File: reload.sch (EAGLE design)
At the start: 19 parts, among them IC1 LP2950, IC2 LP2950Z, Q1 BTS117

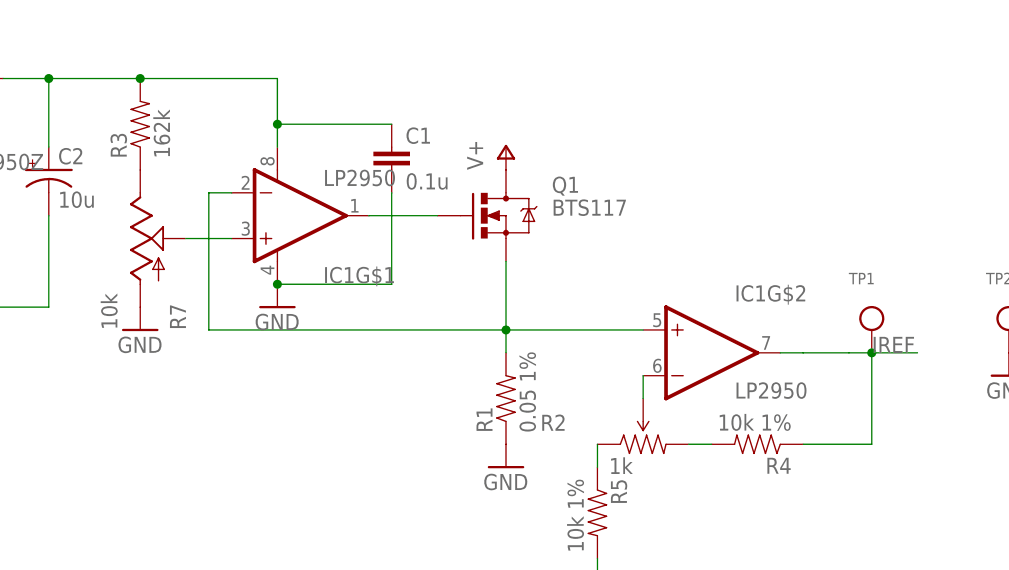
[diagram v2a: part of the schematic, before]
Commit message: Added a second BoM for 10A version.
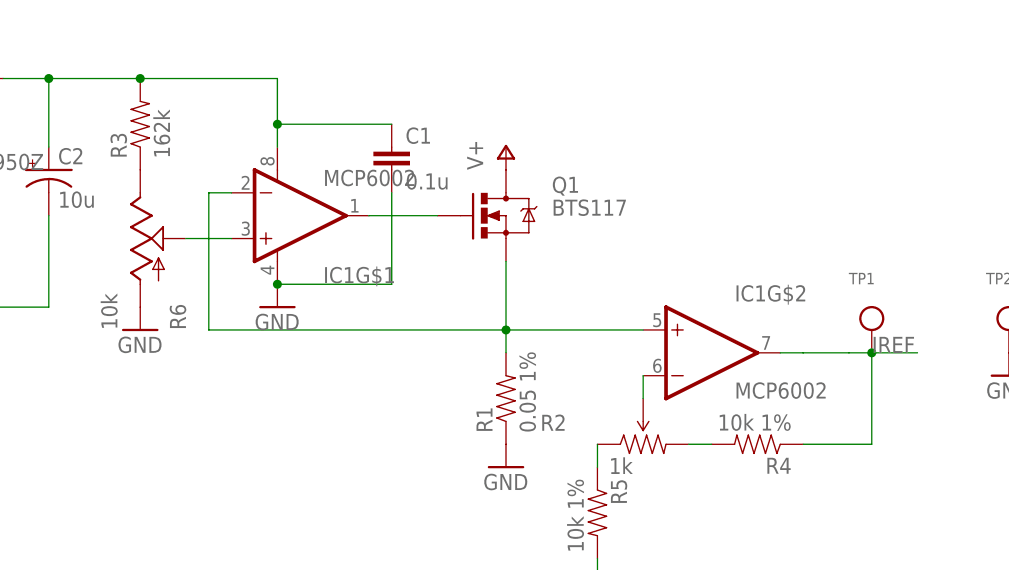
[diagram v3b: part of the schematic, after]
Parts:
- IC1: value LP2950 -> MCP6002
- renumbered R7 to R6
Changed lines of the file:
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@@
 </classes>
 <parts>
-<part name="IC1" library="SparkFun-AnalogIC" deviceset="LM358" device="" value="LP2950"/>
+<part name="IC1" library="SparkFun-AnalogIC" deviceset="LM358" device="" value="MCP6002"/>
 <part name="R1" library="SparkFun-Passives" deviceset="RESISTOR" device="PTH-1W" value="0.05 1%"/>
 <part name="Q1" library="SparkFun-DiscreteSemi" deviceset="MOSFET-NCHANNEL" device="PTH2" value="BTS117"/>
@@
 <part name="GND1" library="supply1" deviceset="GND" device=""/>
 <part name="GND2" library="supply1" deviceset="GND" device=""/>
-<part name="R7" library="SparkFun-Electromechanical" deviceset="POT" device="" value="10k"/>
+<part name="R6" library="SparkFun-Electromechanical" deviceset="POT" device="" value="10k"/>
 <part name="GND3" library="supply1" deviceset="GND" device=""/>
 <part name="R3" library="SparkFun-Passives" deviceset="RESISTOR" device="AXIAL-0.3" value="162k"/>
@@
 <instance part="GND1" gate="1" x="58.42" y="7.62"/>
 <instance part="GND2" gate="1" x="33.02" y="25.4"/>
-<instance part="R7" gate="G$1" x="17.78" y="33.02"/>
+<instance part="R6" gate="G$1" x="17.78" y="33.02"/>
 <instance part="GND3" gate="1" x="17.78" y="22.86"/>
 <instance part="R3" gate="G$1" x="17.78" y="45.72" rot="R90"/>
@@
 </segment>
 <segment>
-<pinref part="R7" gate="G$1" pin="A"/>
+<pinref part="R6" gate="G$1" pin="A"/>
 <pinref part="GND3" gate="1" pin="GND"/>
 </segment>
@@
 <net name="N$3" class="0">
 <segment>
-<pinref part="R7" gate="G$1" pin="E"/>
+<pinref part="R6" gate="G$1" pin="E"/>
 <pinref part="R3" gate="G$1" pin="1"/>
 </segment>
@@
 <net name="N$4" class="0">
 <segment>
-<pinref part="R7" gate="G$1" pin="S"/>
+<pinref part="R6" gate="G$1" pin="S"/>
 <pinref part="IC1" gate="G$1" pin="+IN"/>
 <wire x1="22.86" y1="33.02" x2="27.94" y2="33.02" width="0.1524" layer="91"/>

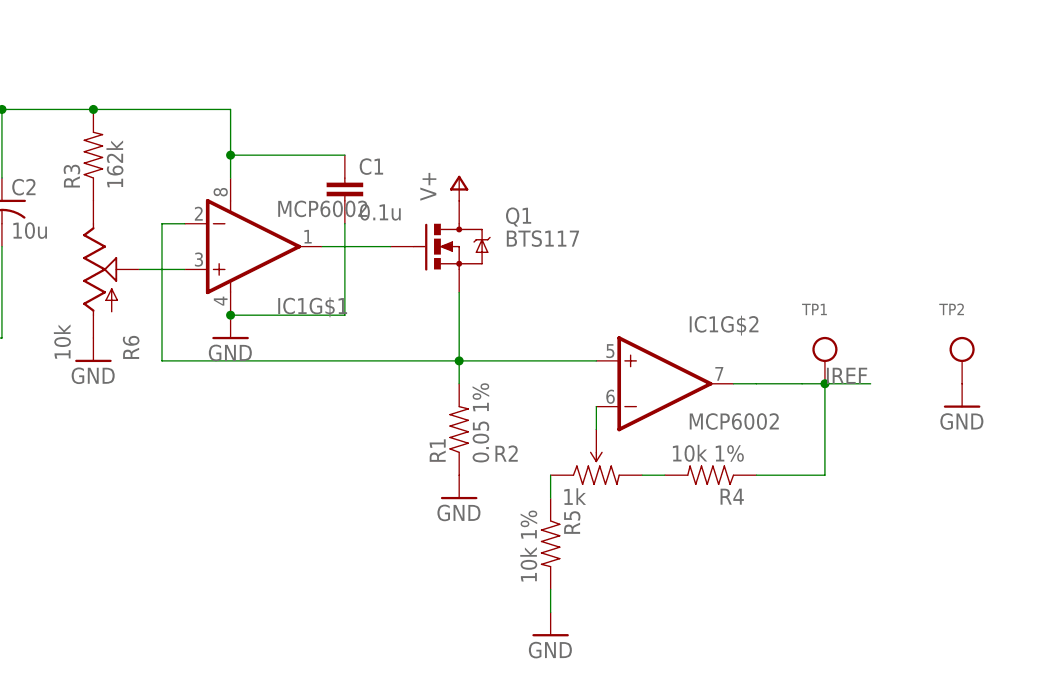
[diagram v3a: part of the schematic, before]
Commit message: Added series resistor for FET output.
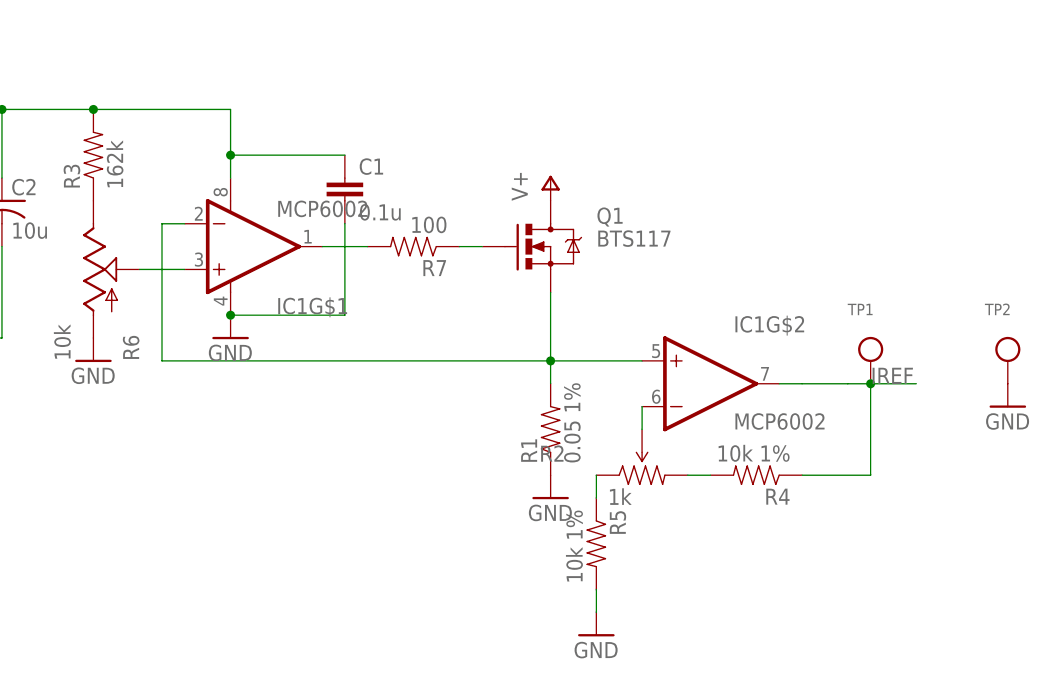
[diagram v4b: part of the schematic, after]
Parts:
- added R7: 100, SparkFun-Passives:RESISTORAXIAL-0.3
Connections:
- new net N$9: Q1.G, R7.1
- net N$1: now also R7.2; no longer Q1.G
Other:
- moved on the sheet: IC1G$2, Q1, R1, R2, R4, R5, TP1, TP2
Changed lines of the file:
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@@
 <part name="KK1" library="nickparts" deviceset="SK129-PAD" device=""/>
 <part name="R2" library="nickparts" deviceset="TRIMPOT" device="3MM-2" value="1k"/>
+<part name="R7" library="SparkFun-Passives" deviceset="RESISTOR" device="AXIAL-0.3" value="100"/>
 </parts>
 <sheets>
@@
 <instances>
 <instance part="IC1" gate="G$1" x="33.02" y="35.56"/>
-<instance part="R1" gate="G$1" x="58.42" y="15.24" rot="R90"/>
-<instance part="Q1" gate="G$1" x="58.42" y="35.56"/>
+<instance part="R1" gate="G$1" x="68.58" y="15.24" rot="R90"/>
+<instance part="Q1" gate="G$1" x="68.58" y="35.56"/>
 <instance part="J1" gate="G$1" x="-22.86" y="78.74" rot="R180"/>
 <instance part="J2" gate="G$1" x="-22.86" y="66.04" rot="R180"/>
 <instance part="JP1" gate="G$1" x="-27.94" y="71.12"/>
-<instance part="P+1" gate="1" x="58.42" y="43.18"/>
-<instance part="GND1" gate="1" x="58.42" y="7.62"/>
+<instance part="P+1" gate="1" x="68.58" y="43.18"/>
+<instance part="GND1" gate="1" x="68.58" y="7.62"/>
 <instance part="GND2" gate="1" x="33.02" y="25.4"/>
 <instance part="R6" gate="G$1" x="17.78" y="33.02"/>
@@
 <instance part="P+3" gate="1" x="-38.1" y="53.34"/>
 <instance part="C1" gate="G$1" x="45.72" y="40.64"/>
-<instance part="IC1" gate="G$2" x="81.28" y="20.32"/>
-<instance part="R5" gate="G$1" x="68.58" y="2.54" rot="R270"/>
-<instance part="GND5" gate="1" x="68.58" y="-7.62"/>
-<instance part="TP1" gate="G$1" x="99.06" y="20.32"/>
-<instance part="TP2" gate="G$1" x="114.3" y="20.32"/>
-<instance part="GND6" gate="1" x="114.3" y="17.78"/>
-<instance part="R4" gate="G$1" x="86.36" y="10.16" rot="R180"/>
+<instance part="IC1" gate="G$2" x="86.36" y="20.32"/>
+<instance part="R5" gate="G$1" x="73.66" y="2.54" rot="R270"/>
+<instance part="GND5" gate="1" x="73.66" y="-7.62"/>
+<instance part="TP1" gate="G$1" x="104.14" y="20.32"/>
+<instance part="TP2" gate="G$1" x="119.38" y="20.32"/>
+<instance part="GND6" gate="1" x="119.38" y="17.78"/>
+<instance part="R4" gate="G$1" x="91.44" y="10.16" rot="R180"/>
 <instance part="P+4" gate="1" x="-17.78" y="83.82"/>
 <instance part="GND7" gate="1" x="-17.78" y="60.96"/>
@@
 <instance part="C3" gate="G$1" x="-20.32" y="40.64"/>
 <instance part="KK1" gate="G$1" x="17.78" y="68.58"/>
-<instance part="R2" gate="R?" x="73.66" y="10.16"/>
+<instance part="R2" gate="R?" x="78.74" y="10.16"/>
+<instance part="R7" gate="G$1" x="53.34" y="35.56" rot="R180"/>
 </instances>
 <busses>
 </busses>
 <nets>
-<net name="N$1" class="0">
-<segment>
-<pinref part="IC1" gate="G$1" pin="OUT"/>
-<pinref part="Q1" gate="G$1" pin="G"/>
-<wire x1="43.18" y1="35.56" x2="50.8" y2="35.56" width="0.1524" layer="91"/>
-</segment>
-</net>
 <net name="V+" class="0">
 <segment>
@@
 <pinref part="Q1" gate="G$1" pin="S"/>
 <pinref part="R1" gate="G$1" pin="2"/>
-<wire x1="58.42" y1="20.32" x2="58.42" y2="22.86" width="0.1524" layer="91"/>
-<wire x1="58.42" y1="22.86" x2="58.42" y2="30.48" width="0.1524" layer="91"/>
-<wire x1="58.42" y1="22.86" x2="25.4" y2="22.86" width="0.1524" layer="91"/>
+<wire x1="68.58" y1="20.32" x2="68.58" y2="22.86" width="0.1524" layer="91"/>
+<wire x1="68.58" y1="22.86" x2="68.58" y2="30.48" width="0.1524" layer="91"/>
+<wire x1="68.58" y1="22.86" x2="25.4" y2="22.86" width="0.1524" layer="91"/>
 <wire x1="25.4" y1="22.86" x2="25.4" y2="38.1" width="0.1524" layer="91"/>
-<junction x="58.42" y="22.86"/>
+<junction x="68.58" y="22.86"/>
 <pinref part="IC1" gate="G$1" pin="-IN"/>
 <wire x1="25.4" y1="38.1" x2="27.94" y2="38.1" width="0.1524" layer="91"/>
 <pinref part="IC1" gate="G$2" pin="+IN"/>
-<wire x1="58.42" y1="22.86" x2="73.66" y2="22.86" width="0.1524" layer="91"/>
+<wire x1="68.58" y1="22.86" x2="78.74" y2="22.86" width="0.1524" layer="91"/>
 </segment>
 </net>
@@
 <pinref part="R5" gate="G$1" pin="2"/>
 <pinref part="GND5" gate="1" pin="GND"/>
-<wire x1="68.58" y1="-2.54" x2="68.58" y2="-5.08" width="0.1524" layer="91"/>
+<wire x1="73.66" y1="-2.54" x2="73.66" y2="-5.08" width="0.1524" layer="91"/>
 </segment>
 <segment>
@@
 <segment>
 <pinref part="IC1" gate="G$2" pin="OUT"/>
-<wire x1="88.9" y1="20.32" x2="91.44" y2="20.32" width="0.1524" layer="91"/>
-<wire x1="91.44" y1="20.32" x2="96.52" y2="20.32" width="0.1524" layer="91"/>
-<wire x1="99.06" y1="10.16" x2="99.06" y2="20.32" width="0.1524" layer="91"/>
-<wire x1="99.06" y1="20.32" x2="96.52" y2="20.32" width="0.1524" layer="91"/>
-<wire x1="99.06" y1="20.32" x2="104.14" y2="20.32" width="0.1524" layer="91"/>
-<junction x="99.06" y="20.32"/>
-<label x="99.06" y="20.32" size="1.778" layer="95"/>
+<wire x1="93.98" y1="20.32" x2="96.52" y2="20.32" width="0.1524" layer="91"/>
+<wire x1="96.52" y1="20.32" x2="101.6" y2="20.32" width="0.1524" layer="91"/>
+<wire x1="104.14" y1="10.16" x2="104.14" y2="20.32" width="0.1524" layer="91"/>
+<wire x1="104.14" y1="20.32" x2="101.6" y2="20.32" width="0.1524" layer="91"/>
+<wire x1="104.14" y1="20.32" x2="109.22" y2="20.32" width="0.1524" layer="91"/>
+<junction x="104.14" y="20.32"/>
+<label x="104.14" y="20.32" size="1.778" layer="95"/>
 <pinref part="TP1" gate="G$1" pin="P$1"/>
 <pinref part="R4" gate="G$1" pin="1"/>
-<wire x1="91.44" y1="10.16" x2="99.06" y2="10.16" width="0.1524" layer="91"/>
+<wire x1="96.52" y1="10.16" x2="104.14" y2="10.16" width="0.1524" layer="91"/>
 </segment>
 </net>
@@
 <segment>
 <pinref part="R4" gate="G$1" pin="2"/>
-<wire x1="81.28" y1="10.16" x2="78.74" y2="10.16" width="0.1524" layer="91"/>
+<wire x1="86.36" y1="10.16" x2="83.82" y2="10.16" width="0.1524" layer="91"/>
 <pinref part="R2" gate="R?" pin="CW"/>
 </segment>
@@
 <pinref part="IC1" gate="G$2" pin="-IN"/>
 <pinref part="R2" gate="R?" pin="WIPER"/>
-<wire x1="73.66" y1="17.78" x2="73.66" y2="15.24" width="0.1524" layer="91"/>
+<wire x1="78.74" y1="17.78" x2="78.74" y2="15.24" width="0.1524" layer="91"/>
 </segment>
 </net>
@@
 <pinref part="R5" gate="G$1" pin="1"/>
 <pinref part="R2" gate="R?" pin="CCW"/>
-<wire x1="68.58" y1="7.62" x2="68.58" y2="10.16" width="0.1524" layer="91"/>
-</segment>
-</net>
+<wire x1="73.66" y1="7.62" x2="73.66" y2="10.16" width="0.1524" layer="91"/>
+</segment>
+</net>
+<net name="N$1" class="0">
+<segment>
+<pinref part="IC1" gate="G$1" pin="OUT"/>
+<pinref part="R7" gate="G$1" pin="2"/>
+<wire x1="48.26" y1="35.56" x2="43.18" y2="35.56" width="0.1524" layer="91"/>
+</segment>
+</net>
+<net name="N$9" class="0">
+<segment>
+<pinref part="R7" gate="G$1" pin="1"/>
+<pinref part="Q1" gate="G$1" pin="G"/>
+<wire x1="58.42" y1="35.56" x2="60.96" y2="35.56" width="0.1524" layer="91"/>
+</segment>
+</net>

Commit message: Tweaks to schematic.
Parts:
- R6: device SparkFun-Electromechanical:POT -> nickparts:POT
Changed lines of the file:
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@@
 <part name="GND1" library="supply1" deviceset="GND" device=""/>
 <part name="GND2" library="supply1" deviceset="GND" device=""/>
-<part name="R6" library="SparkFun-Electromechanical" deviceset="POT" device="" value="10k"/>
+<part name="R6" library="nickparts" deviceset="POT" device="" value="10k"/>
 <part name="GND3" library="supply1" deviceset="GND" device=""/>
 <part name="R3" library="SparkFun-Passives" deviceset="RESISTOR" device="AXIAL-0.3" value="162k"/>

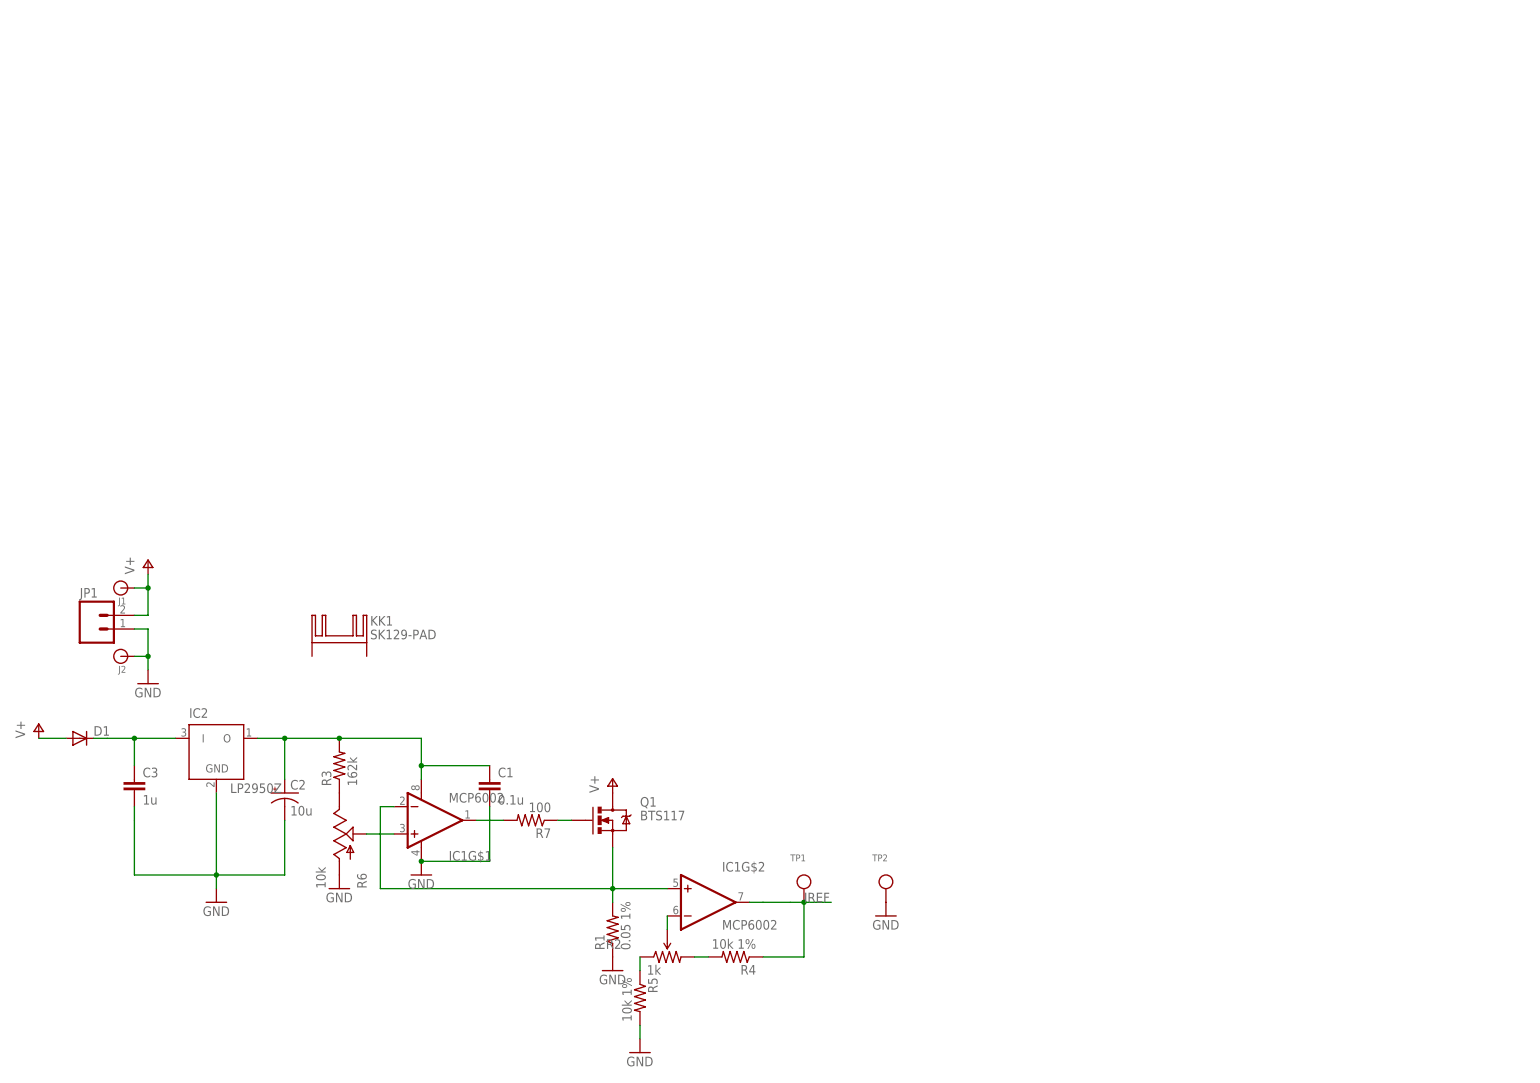
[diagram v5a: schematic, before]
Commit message: Improved schematic layout.
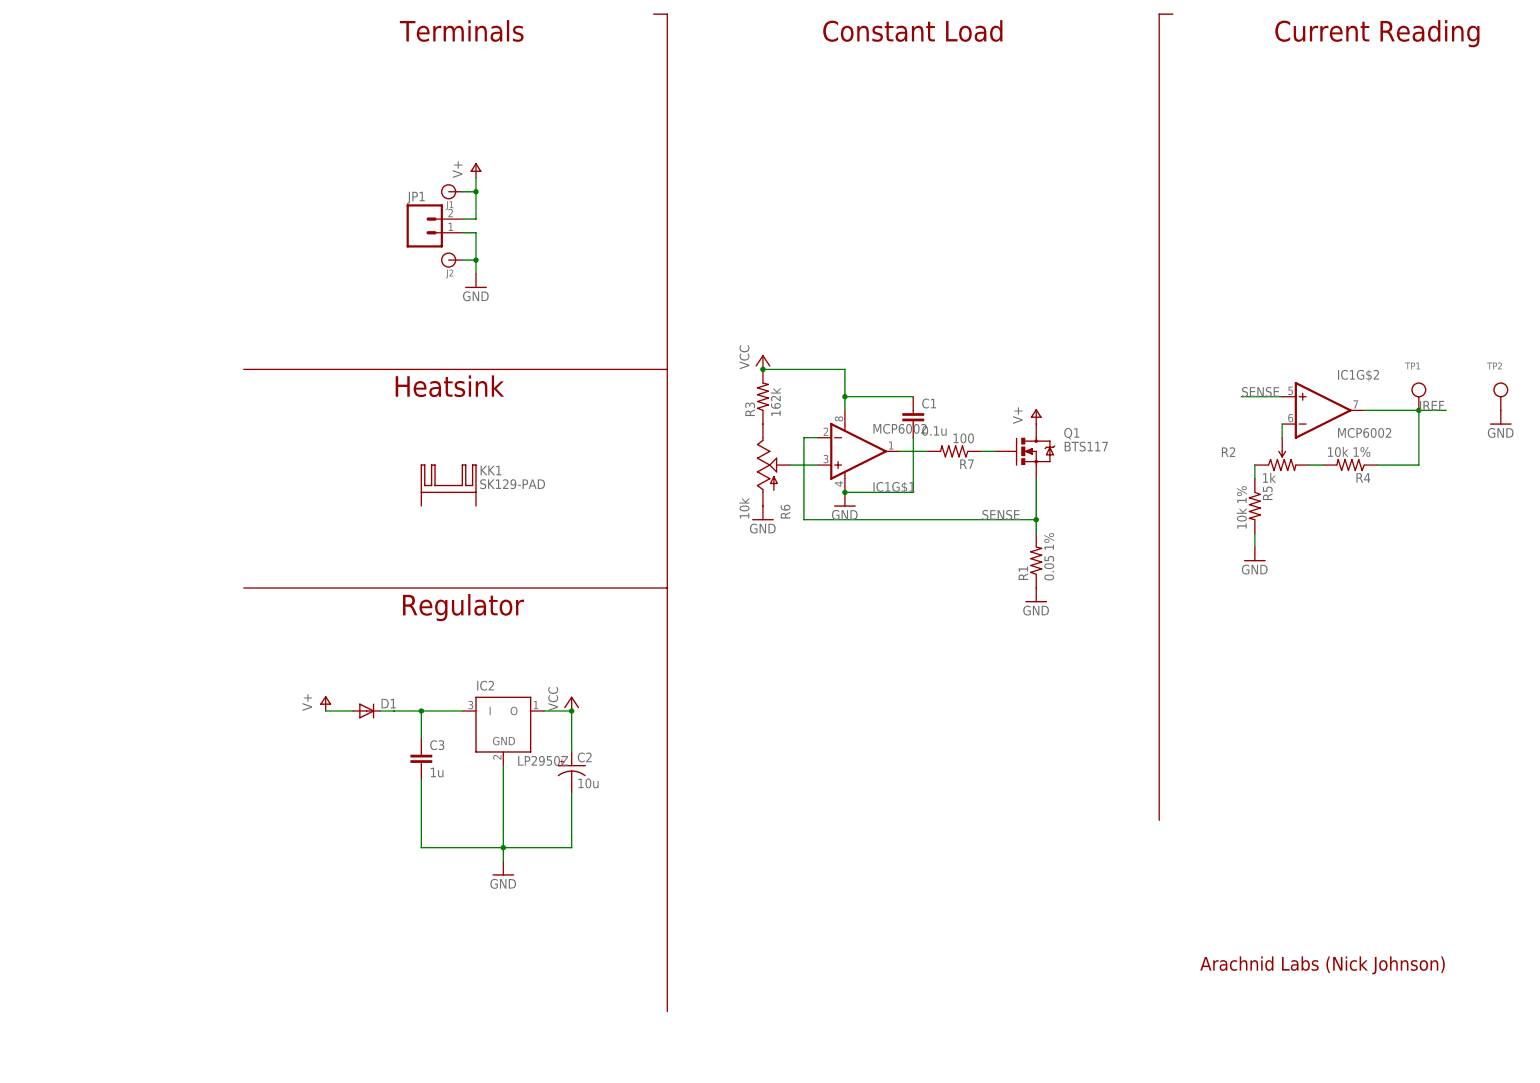
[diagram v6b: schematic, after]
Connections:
- net 3V renamed VCC
- net N$2 renamed SENSE
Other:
- note added: "Arachnid Labs (Nick Johnson)"
- note added: "Constant Load"
- note added: "Current Reading"
- note added: "Heatsink"
- note added: "Regulator"
- note added: "Terminals"
- moved on the sheet: C1, C2, C3, D1, IC1G$1, IC1G$2, IC2, J1, J2, JP1, KK1, Q1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
